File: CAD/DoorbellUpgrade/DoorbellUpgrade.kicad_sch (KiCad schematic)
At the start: 13 parts, among them J1 Klingel Haus, J2 Klingel Etage, J3 Türöffner, J4 Speaker, U1 CNY17-3, U2 CNY17-3, U3 ESP32-DEVKITC

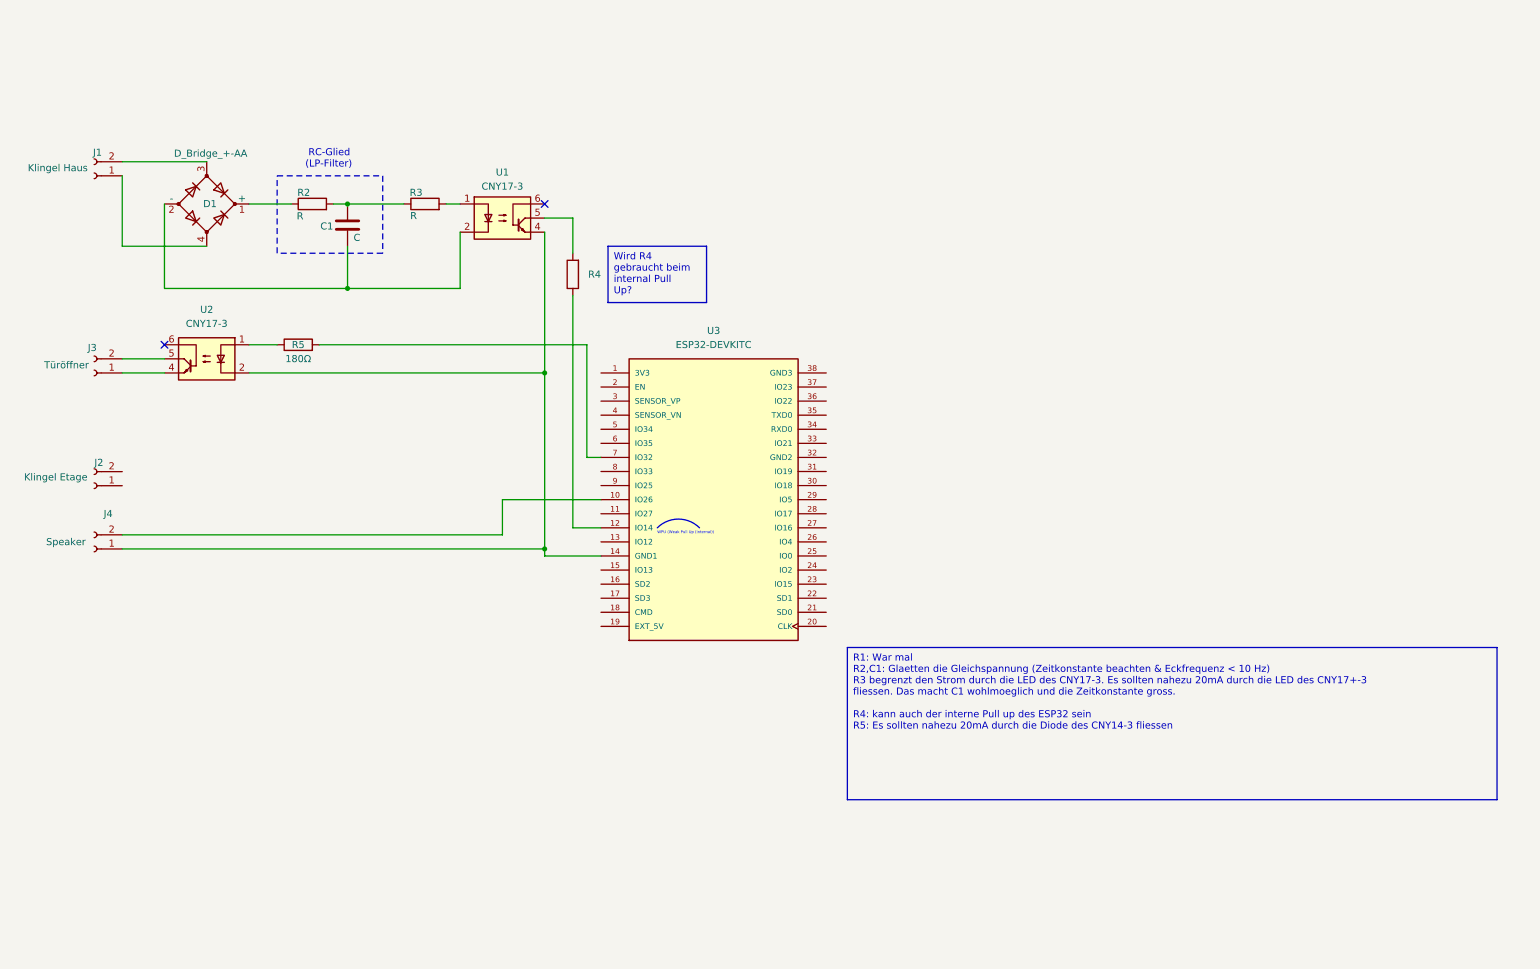
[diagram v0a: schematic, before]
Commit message: change CNY17 to PC829
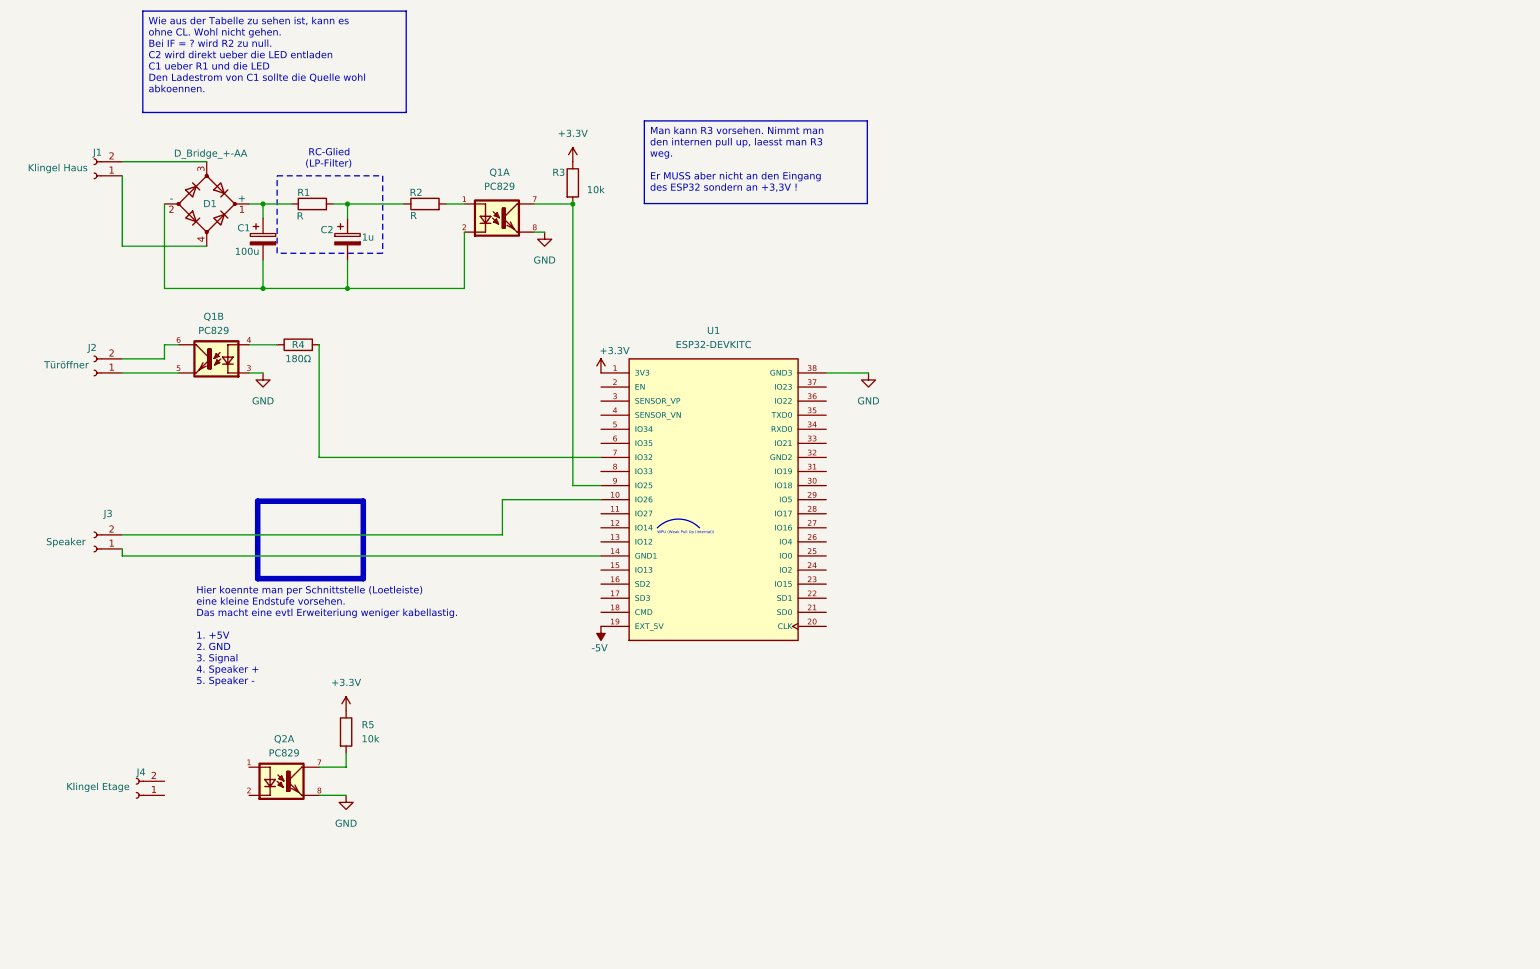
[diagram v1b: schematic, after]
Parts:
- removed C1: C, Capacitor_SMD:C_0504_1310Metric, symbol Device:C
- removed R4: R, symbol Device:R
- removed U1, U2: CNY17-3, symbol Isolator:CNY17-3
- added C1: 100u, symbol Device:C_Polarized
- added C2: 1u, symbol Device:C_Polarized
- added Q1, Q2: PC829, symbol PC829:PC829
- added R3, R5: 10k, symbol Device:R
- renumbered J3 to J2, J4 to J3, J2 to J4, R2 to R1, R3 to R2, R5 to R4, U3 to U1
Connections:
- net at R1.2, R2.1: now also C2.1
- net at R2.2: now also Q1.1
- net at R4.1: now also Q1.4
- net at J2.1 (Pin_1): now also Q1.5
- net at J2.2 (Pin_2): now also Q1.6
- net at D1.2 (-): now also C1.2, C2.2, Q1.2
- net at D1.1 (+), R1.1: now also C1.1
- net +3.3V: now reaches U1.1 (3V3)
- net +3.3V: now also R3.1, R5.1
- net -5V: now reaches U1.19 (EXT_5V)
- net GND: now reaches U1.38 (GND3)
- net GND: now also Q1.3, Q1.8, Q2.8
- net at U1.9 (IO25): now also Q1.7, R3.2
- new net: Q2.7, R5.2
- no-connect marks 2 -> 0
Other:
- note added: "Hier koennte man per Schnittstelle (Loetleiste) eine kleine Endstufe vorsehen. Das macht eine evtl Erweiteriung weniger kabellastig. 1. +5V 2. GND 3. Signal 4. Speaker + 5. Speaker -"
- moved on the sheet: J4

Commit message: small change in values
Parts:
- C2: value 1u -> 10u
- R1: value R -> 220
- R2: value R -> 0
- R4: value 180Ω -> 100
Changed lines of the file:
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@@
       (effects (font (size 1.27 1.27)))
     )
-    (property "Value" "R" (at 88.1126 60.5536 90)
+    (property "Value" "0" (at 90.17 60.96 90)
       (effects (font (size 1.27 1.27)))
     )
@@
       (effects (font (size 1.27 1.27)))
     )
-    (property "Value" "180Ω" (at 67.31 86.36 90)
+    (property "Value" "100" (at 67.31 86.36 90)
       (effects (font (size 1.27 1.27)))
     )
@@
   (symbol (lib_id "Device:R") (at 69.85 58.42 90) (unit 1)
     (in_bom yes) (on_board yes) (dnp no)
-    (property "Reference" "R1" (at 68.3006 56.3626 90)
-      (effects (font (size 1.27 1.27)))
-    )
-    (property "Value" "R" (at 67.6402 60.6044 90)
+    (property "Reference" "R1" (at 69.85 55.88 90)
+      (effects (font (size 1.27 1.27)))
+    )
+    (property "Value" "220" (at 69.85 60.96 90)
       (effects (font (size 1.27 1.27)))
     )
@@
       (effects (font (size 1.27 1.27)) (justify left))
     )
-    (property "Value" "1u" (at 78.7908 64.4398 0)
-      (effects (font (size 1.27 1.27)) (justify left))
-    )
+    (property "Value" "10u" (at 71.12 67.31 0)
+      (effects (font (size 1.27 1.27)) (justify left))
+    )

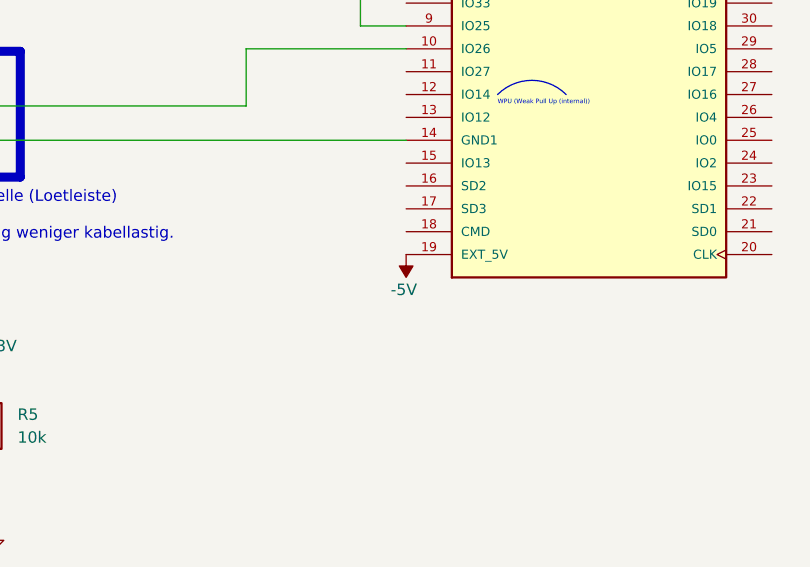
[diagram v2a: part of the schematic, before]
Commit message: correct symbol -5V at esp32 pin 19 to +5V
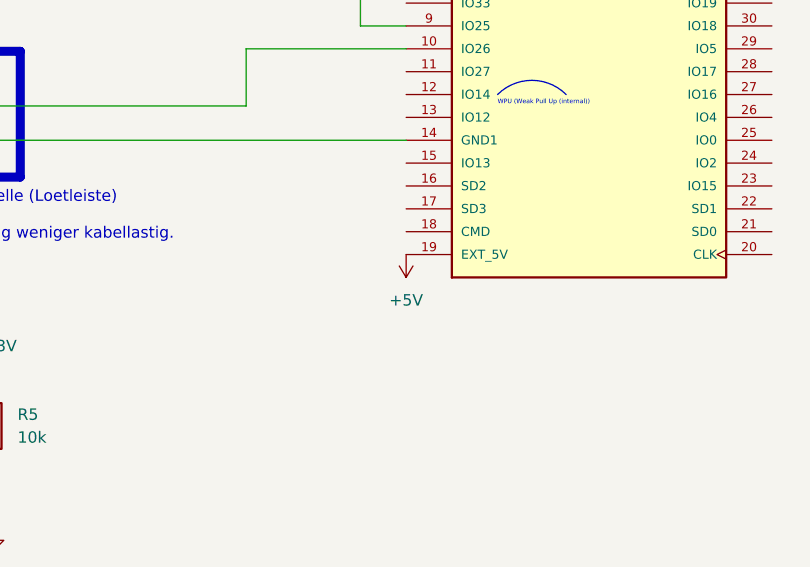
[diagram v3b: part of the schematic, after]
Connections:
- net -5V renamed +5V
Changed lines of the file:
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@@
-    )
-  )
-  (symbol (lib_id "power:-5V") (at 121.92 134.62 180) (unit 1)
-    (in_bom yes) (on_board yes) (dnp no)
-    (property "Reference" "#PWR06" (at 121.92 137.16 0)
-      (effects (font (size 1.27 1.27)) hide)
-    )
-    (property "Value" "-5V" (at 121.666 138.5316 0)
-      (effects (font (size 1.27 1.27)))
-    )
-    (property "Footprint" "" (at 121.92 134.62 0)
-      (effects (font (size 1.27 1.27)) hide)
-    )
-    (property "Datasheet" "" (at 121.92 134.62 0)
-      (effects (font (size 1.27 1.27)) hide)
-    )
-    (pin "1")
-    (instances
-      (project "DoorbellUpgrade"
-        (path "/092c1a95-a0ce-445b-abe2-a93e0f430456"
-          (reference "#PWR06") (unit 1)
-        )
-      )
     )
   )
@@
         )
       )
+    )
+  )
+  (symbol (lib_id "power:+5V") (at 121.92 134.62 180) (unit 1)
+    (in_bom yes) (on_board yes) (dnp no) (fields_autoplaced)
+    (property "Reference" "#PWR06" (at 121.92 130.81 0)
+      (effects (font (size 1.27 1.27)) hide)
+    )
+    (property "Value" "+5V" (at 121.92 139.7 0)
+      (effects (font (size 1.27 1.27)))
+    )
+    (property "Footprint" "" (at 121.92 134.62 0)
+      (effects (font (size 1.27 1.27)) hide)
+    )
+    (property "Datasheet" "" (at 121.92 134.62 0)
+      (effects (font (size 1.27 1.27)) hide)
+    )
+    (pin "1")
+    (instances
+      (project "DoorbellUpgrade"
+        (path "/092c1a95-a0ce-445b-abe2-a93e0f430456"
+          (reference "#PWR06") (unit 1)
+        )
+      )

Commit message: first schematic
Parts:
- added D?: 1N4007, Diode_THT:D_DO-41_SOD81_P10.16mm_Horizontal, symbol Diode:1N4007
- added K?: DIL-Relais 5V, Relay_THT:Relay_StandexMeder_DIP_LowProfile, symbol Relay:DIPxx-1Axx-12x
- added Q?: BC550, Package_TO_SOT_THT:TO-92_Inline, symbol Transistor_BJT:BC550
- added R?: 1k, symbol Device:R
- J1: value Klingel Haus -> Bell Street
- J2: value Türöffner -> Street open buzzer
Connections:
- net +5V: now also D?.1 (K), K?.13, K?.2
- net GND: now also Q?.3 (E)
- net at R4.2: no longer U1.7 (IO32)
- net at J2.1 (Pin_1): now also K?.7, K?.8; no longer Q1.5
- net at J2.2 (Pin_2): now also K?.1, K?.14; no longer Q1.6
- new net: D?.2 (A), K?.6, Q?.1 (C)
- new net: Q?.2 (B), R?.1
- new net: R?.2, U1.7 (IO32)
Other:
- moved on the sheet: J2, J3, J4, Q1B, Q2A, R4, R5
